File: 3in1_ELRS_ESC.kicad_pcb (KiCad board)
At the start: 2 copper layers, 35 x 35 mm, 93 parts, among them P1 SM08B-SRSS-TB(LF)(SN), Q1 SP40N03GNJ, Q10 SP40N03GNJ, Q11 SP40N03GNJ, Q12 SP40N03GNJ, Q2 SP40N03GNJ, Q3 SP40N03GNJ, Q4 SP40N03GNJ, Q5 SP40N03GNJ, Q6 SP40N03GNJ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

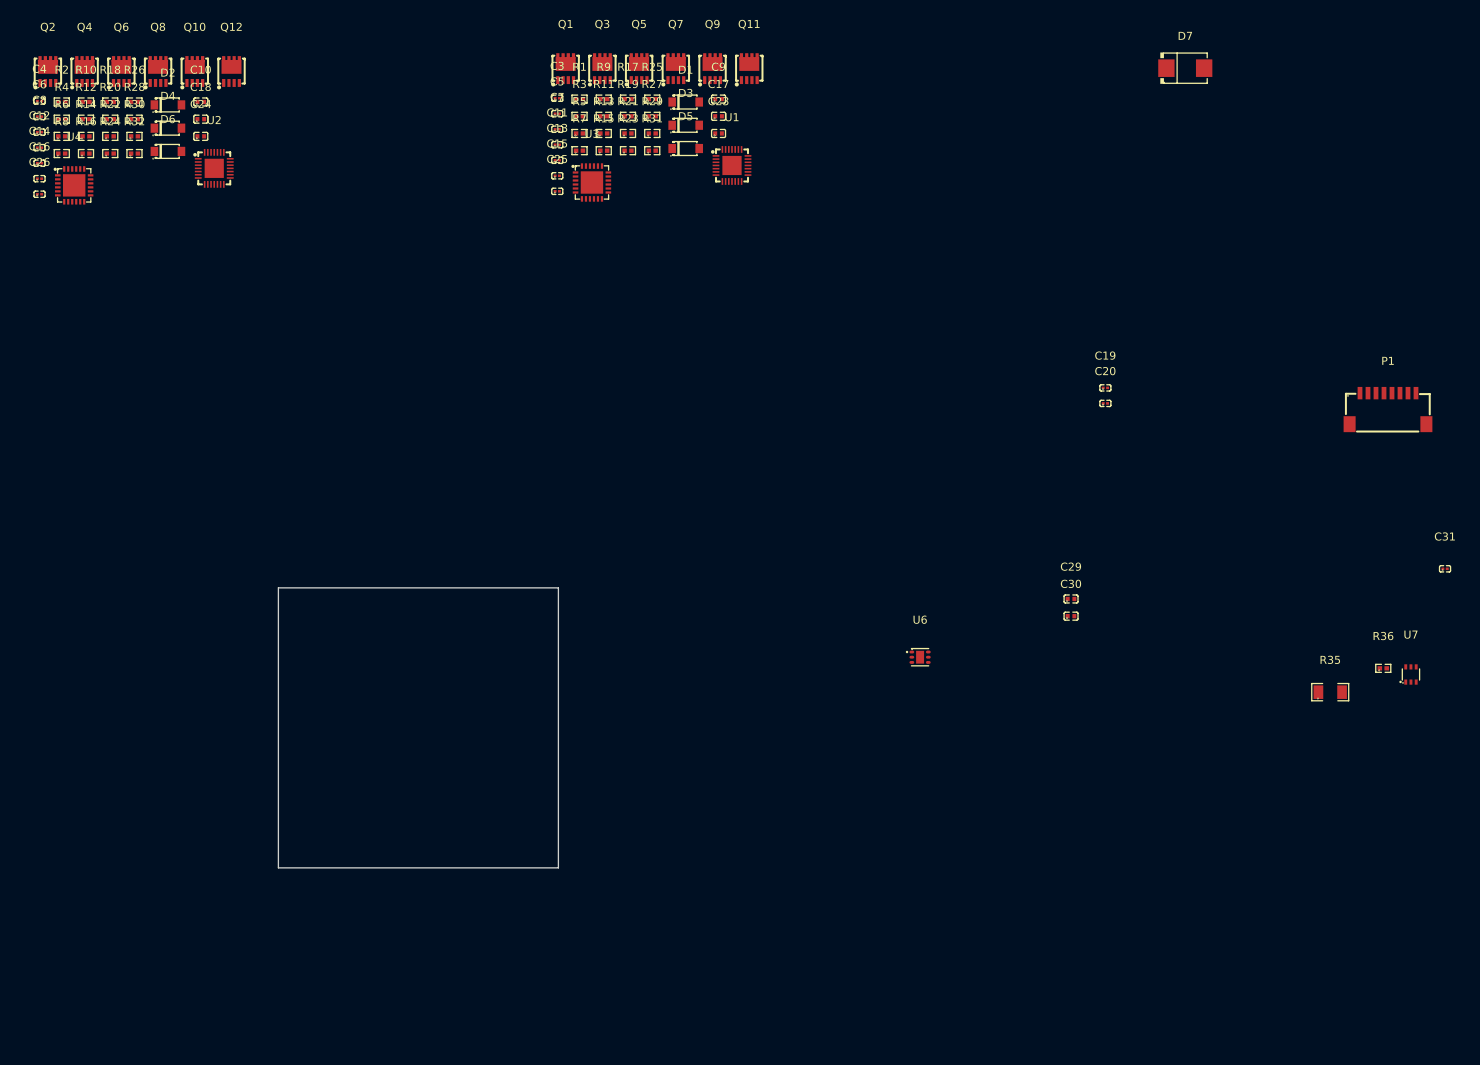
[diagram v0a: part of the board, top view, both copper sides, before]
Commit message: FET's Placed
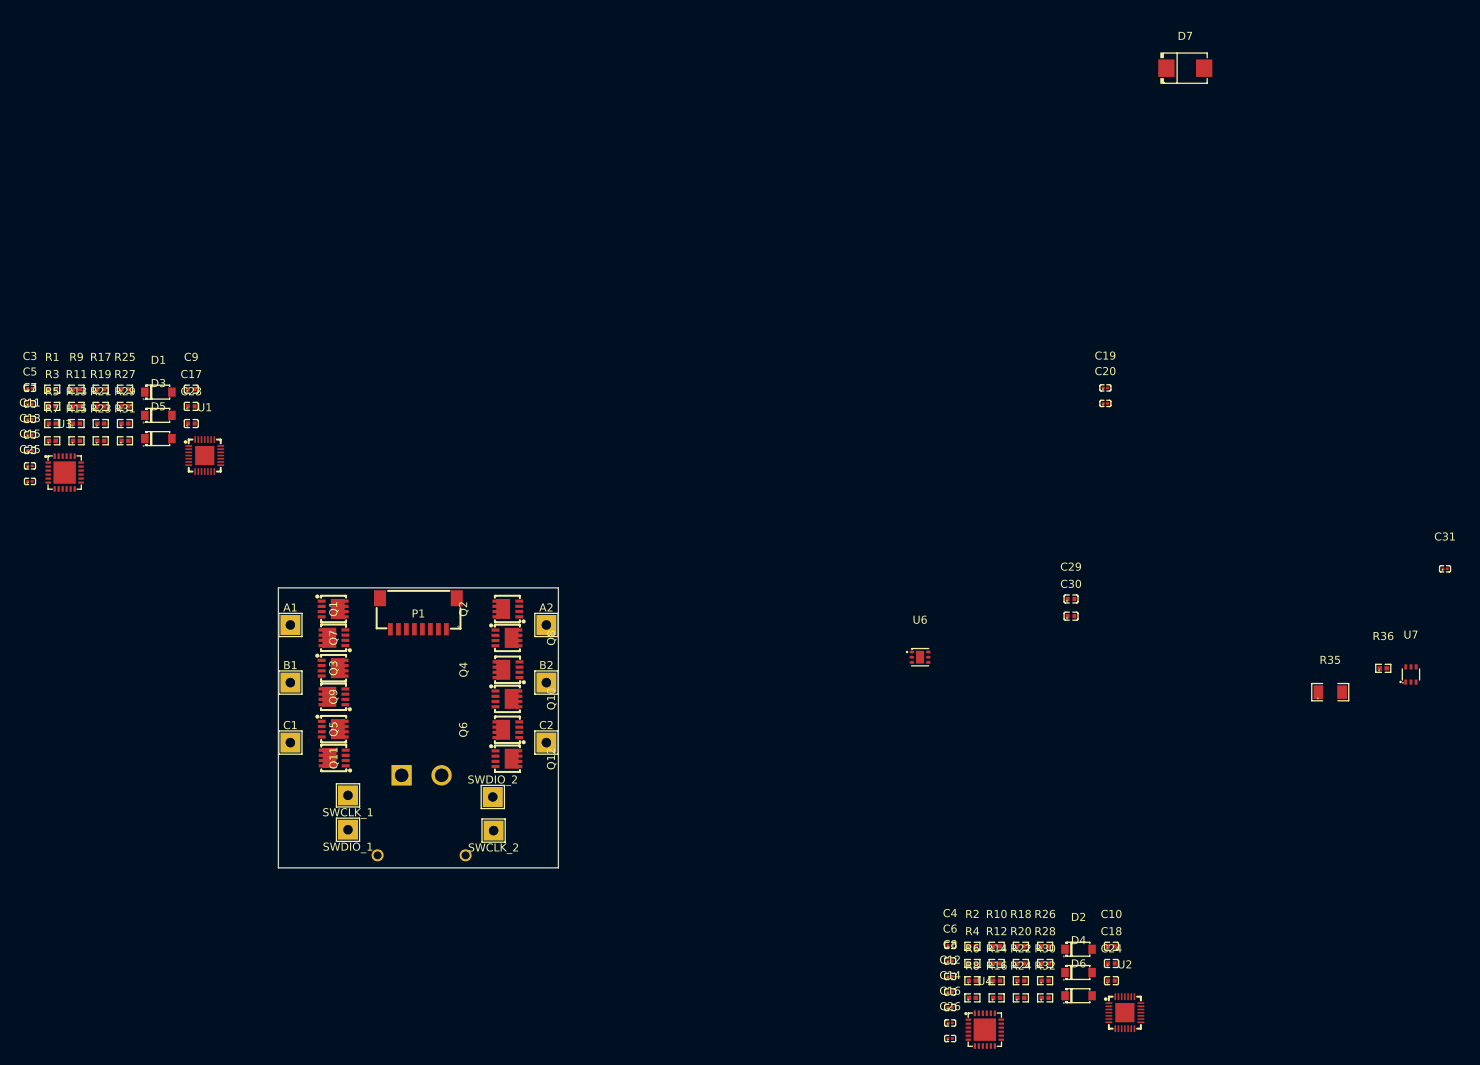
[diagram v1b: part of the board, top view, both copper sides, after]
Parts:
- added A1: Motor 1 - A, TestPoint:TestPoint_THTPad_2.5x2.5mm_Drill1.2mm, F.Cu at (65.0, 102.1)
- added A2: Motor 2 - A, TestPoint:TestPoint_THTPad_2.5x2.5mm_Drill1.2mm, F.Cu at (97.0, 102.1)
- added B1: Motor 1 - B, TestPoint:TestPoint_THTPad_2.5x2.5mm_Drill1.2mm, F.Cu at (65.0, 109.3)
- added B2: Motor 2 - B, TestPoint:TestPoint_THTPad_2.5x2.5mm_Drill1.2mm, F.Cu at (97.0, 109.3)
- added C1: Motor 1 - C, TestPoint:TestPoint_THTPad_2.5x2.5mm_Drill1.2mm, F.Cu at (65.0, 116.8)
- added C2: Motor 2 - C, TestPoint:TestPoint_THTPad_2.5x2.5mm_Drill1.2mm, F.Cu at (97.0, 116.8)
- added J2: XT30PW-M, XT30PW-M:AMASS_XT30PW-M, B.Cu at (81.4, 130.9)
- added SWCLK_1: ~, TestPoint:TestPoint_THTPad_2.5x2.5mm_Drill1.2mm, F.Cu at (72.2, 123.4)
- added SWCLK_2: ~, TestPoint:TestPoint_THTPad_2.5x2.5mm_Drill1.2mm, F.Cu at (90.4, 127.8)
- added SWDIO_1: ~, TestPoint:TestPoint_THTPad_2.5x2.5mm_Drill1.2mm, F.Cu at (72.2, 127.7)
- added SWDIO_2: ~, TestPoint:TestPoint_THTPad_2.5x2.5mm_Drill1.2mm, F.Cu at (90.3, 123.6)
- moved C10 155.2 mm to (167.6, 142.3)
- moved C16 155.2 mm to (147.5, 151.9)
- moved C26 155.2 mm to (147.5, 153.8)
- moved R10 155.2 mm to (153.3, 142.3)
- moved R18 155.2 mm to (156.3, 142.3)
- moved R2 155.2 mm to (150.2, 142.3)
- moved R24 155.2 mm to (156.3, 148.7)
- moved R26 155.2 mm to (159.3, 142.3)
- moved R32 155.2 mm to (159.3, 148.7)
- moved C12 155.2 mm to (147.5, 148.0)
- moved C14 155.2 mm to (147.5, 149.9)
- moved C18 155.2 mm to (167.6, 144.4)
- moved C24 155.2 mm to (167.6, 146.6)
- moved C4 155.2 mm to (147.5, 142.2)
- moved C6 155.2 mm to (147.5, 144.1)
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
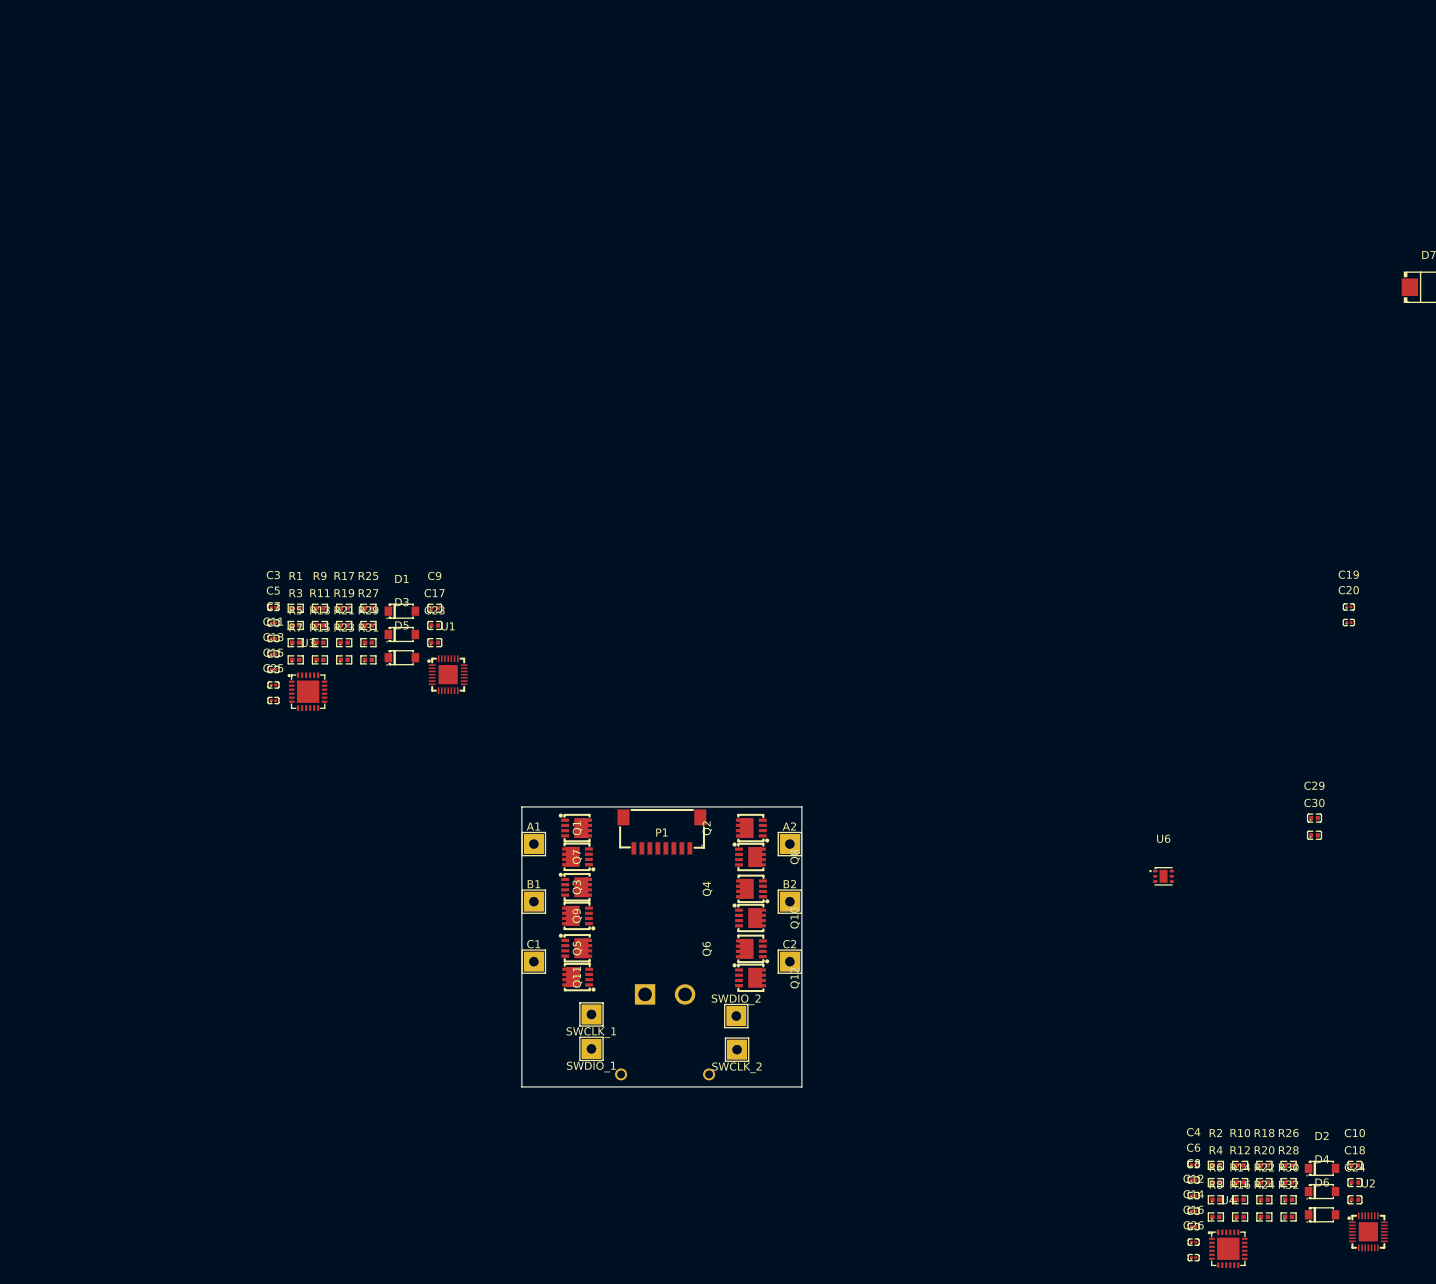
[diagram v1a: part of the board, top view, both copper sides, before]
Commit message: Bridges Placed
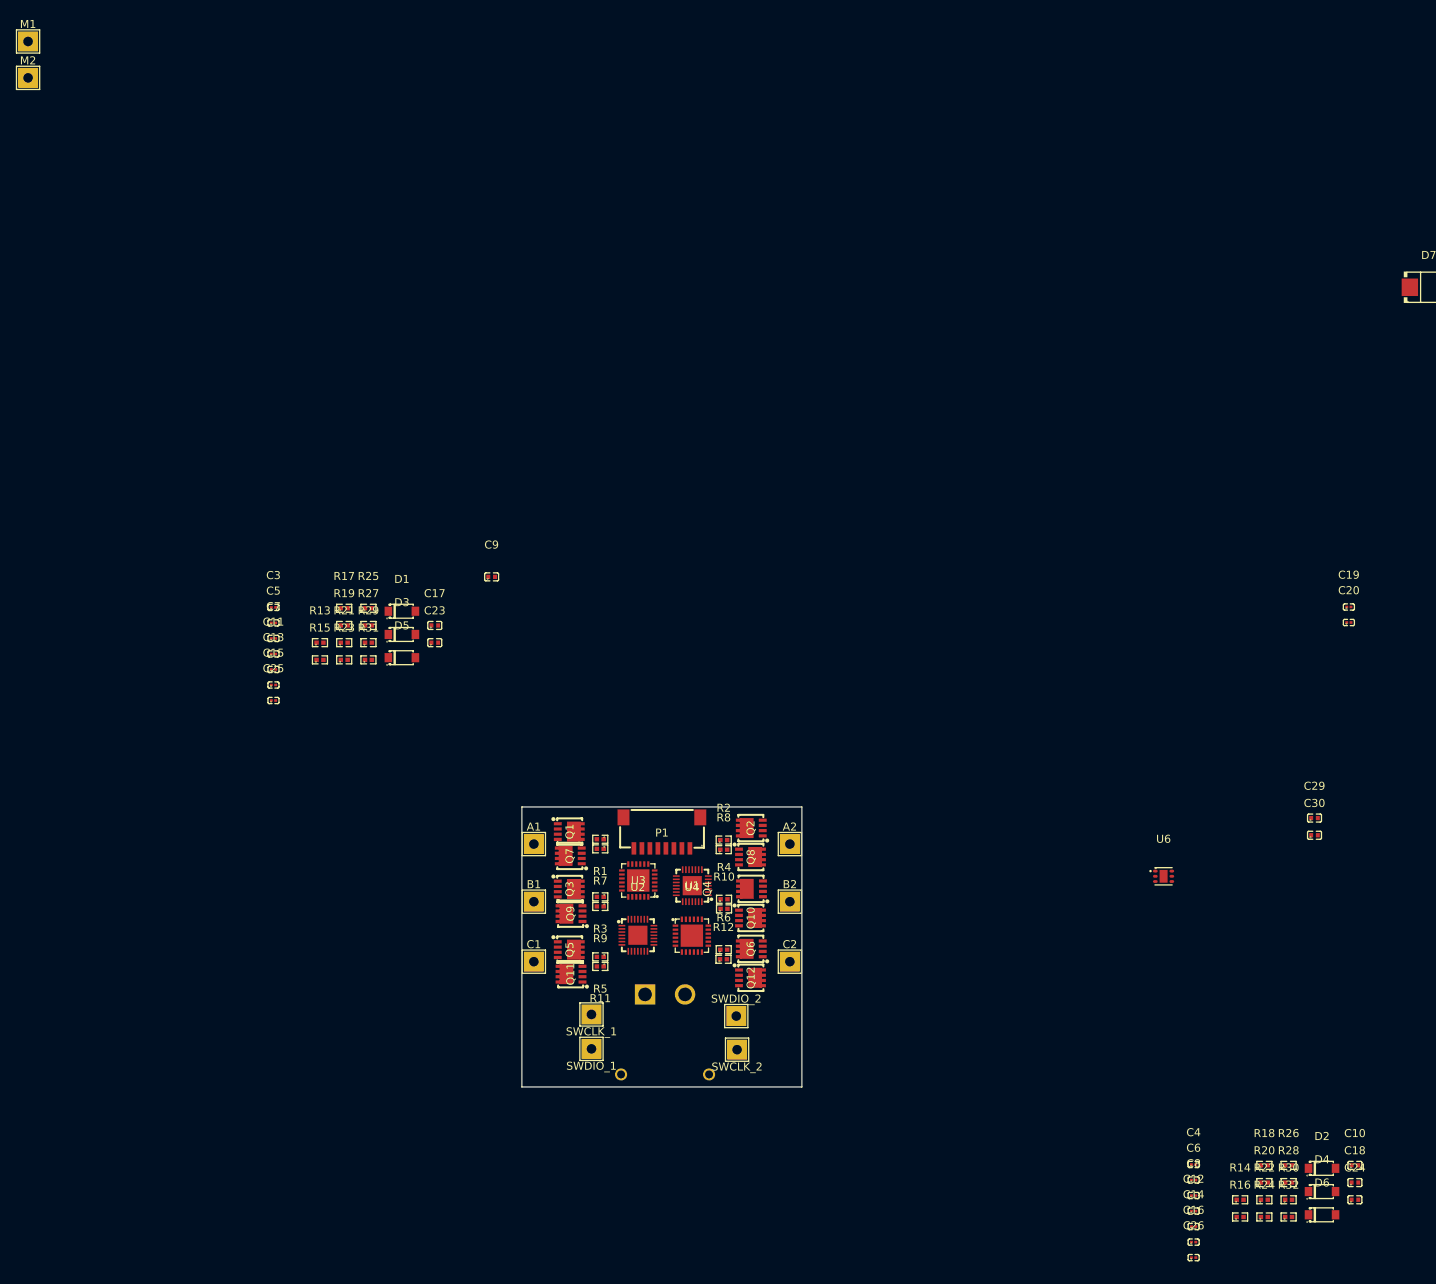
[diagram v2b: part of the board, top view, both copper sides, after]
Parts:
- added M1: ~, TestPoint:TestPoint_THTPad_2.5x2.5mm_Drill1.2mm, F.Cu at (1.77, 1.77)
- added M2: ~, TestPoint:TestPoint_THTPad_2.5x2.5mm_Drill1.2mm, F.Cu at (1.77, 6.33)
- moved U2 98.5 mm to (78.0, 113.5)
- moved U4 77.6 mm to (84.8, 113.5)
- moved R8 76.8 mm to (88.7, 102.8)
- moved R2 73.7 mm to (88.7, 101.6)
- moved R10 72.0 mm to (88.8, 110.2)
- moved R4 71.0 mm to (88.8, 109.0)
- moved R12 70.4 mm to (88.7, 116.5)
- moved R6 69.0 mm to (88.7, 115.3)
- moved R11 55.2 mm to (73.3, 117.4), turned to 180 degrees
- moved R5 54.7 mm to (73.3, 116.2), turned to 180 degrees
- moved R9 51.2 mm to (73.3, 109.9), turned to 180 degrees
- moved R3 51.0 mm to (73.3, 108.7), turned to 180 degrees
- moved R1 47.8 mm to (73.3, 101.5), turned to 180 degrees
- moved U3 47.5 mm to (78.0, 106.7), turned to 180 degrees
- moved R7 44.8 mm to (73.3, 102.7), turned to 180 degrees
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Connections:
- net /ESC 1/GHA renamed /ESC 1/GHA_1
- net /ESC 1/GHB renamed /ESC 1/GHB_1
- net /ESC 1/GHC renamed /ESC 1/GHC_1
- net /ESC 1/GLA renamed /ESC 1/GLA_1
- net /ESC 1/GLB renamed /ESC 1/GLB_1
- net /ESC 1/GLC renamed /ESC 1/GLC_1
- net /ESC 2/GHA renamed /ESC 2/GHA_1
- net /ESC 2/GHB renamed /ESC 2/GHB_1
- net /ESC 2/GHC renamed /ESC 2/GHC_1
- net /ESC 2/GLA renamed /ESC 2/GLA_1
- net /ESC 2/GLB renamed /ESC 2/GLB_1
- net /ESC 2/GLC renamed /ESC 2/GLC_1
- net Net-(Q1-G) renamed /ESC 1/GHA_2
- net Net-(Q10-G) renamed /ESC 2/GLB_2
- net Net-(Q11-G) renamed /ESC 1/GLC_2
- net Net-(Q12-G) renamed /ESC 2/GLC_2
- net Net-(Q2-G) renamed /ESC 2/GHA_2
- net Net-(Q3-G) renamed /ESC 1/GHB_2
- net Net-(Q4-G) renamed /ESC 2/GHB_2
- net Net-(Q5-G) renamed /ESC 1/GHC_2
- net Net-(Q6-G) renamed /ESC 2/GHC_2
- net Net-(Q7-G) renamed /ESC 1/GLA_2
- net Net-(Q8-G) renamed /ESC 2/GLA_2
- net Net-(Q9-G) renamed /ESC 1/GLB_2
